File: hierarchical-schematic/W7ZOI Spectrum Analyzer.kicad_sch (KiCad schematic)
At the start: 0 parts

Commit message: improvements to hierarchical schematic
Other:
- note added: ".options gmin=1e-10 .options abstol=1e-10 .tran 10m 500m"
- note added: ".param Rt=10k set=0.9 .param Rt2=10k set2=0.5 .param Rt3=5k set3=0.5 .param Rt4=10k set4=0.9 .param Rt5=5k set5=0.9 .param Rt6=5k set6=0.5"
- note added: "Settings for Pots"
- note added: "Simulation Commands"
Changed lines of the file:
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@@
     (comment 4 "Original Design By:")
   )
-  (image (at 82.55 54.61) (scale 0.801488)
+  (polyline (pts (xy 307.34 156.21) (xy 307.34 167.64))
+    (stroke (width 0) (type default) (color 0 0 0 0))
+  )
+  (polyline (pts (xy 279.4 156.21) (xy 279.4 151.13))
+    (stroke (width 0) (type default) (color 0 0 0 0))
+  )
+  (polyline (pts (xy 336.55 157.48) (xy 336.55 167.64))
+    (stroke (width 0) (type default) (color 0 0 0 0))
+  )
+  (polyline (pts (xy 336.55 167.64) (xy 309.88 167.64))
+    (stroke (width 0) (type default) (color 0 0 0 0))
+  )
+  (polyline (pts (xy 307.34 151.13) (xy 307.34 156.21))
+    (stroke (width 0) (type default) (color 0 0 0 0))
+  )
+  (polyline (pts (xy 309.88 157.48) (xy 336.55 157.48))
+    (stroke (width 0) (type default) (color 0 0 0 0))
+  )
+  (polyline (pts (xy 279.4 151.13) (xy 307.34 151.13))
+    (stroke (width 0) (type default) (color 0 0 0 0))
+  )
+  (polyline (pts (xy 309.88 157.48) (xy 309.88 167.64))
+    (stroke (width 0) (type default) (color 0 0 0 0))
+  )
+  (polyline (pts (xy 279.4 156.21) (xy 279.4 167.64))
+    (stroke (width 0) (type default) (color 0 0 0 0))
+  )
+  (polyline (pts (xy 307.34 167.64) (xy 279.4 167.64))
+    (stroke (width 0) (type default) (color 0 0 0 0))
+  )
+  (image (at 86.36 158.75) (scale 0.801488)
     (data
       iVBORw0KGgoAAAANSUhEUgAAB8AAAASGCAIAAADZyyOxAAAAA3NCSVQICAjb4U/gAAAACXBIWXMA
@@
     )
   )
-  (hierarchical_label "+15" (shape input) (at 237.49 66.04 0)
-    (effects (font (size 1.27 1.27)) (justify left))
+  (text ".options gmin=1e-10\n.options abstol=1e-10\n.tran 10m 500m"
+    (at 312.42 166.37 0)
+    (effects (font (size 1.27 1.27)) (justify left bottom))
   )
-  (hierarchical_label "-15v" (shape input) (at 237.49 91.44 0)
-    (effects (font (size 1.27 1.27)) (justify left))
+  (text ".param Rt=10k set=0.9\n.param Rt2=10k set2=0.5\n.param Rt3=5k set3=0.5\n.param Rt4=10k set4=0.9\n.param Rt5=5k set5=0.9\n.param Rt6=5k set6=0.5\n"
+    (at 280.67 166.37 0)
+    (effects (font (size 1.27 1.27)) (justify left bottom))
   )
-  (sheet (at 166.37 120.65) (size 33.02 39.37) (fields_autoplaced)
+  (text "Simulation Commands" (at 312.42 160.02 0)
+    (effects (font (size 1.27 1.27) (thickness 0.254) bold) (justify left bottom))
+  )
+  (text "Settings for Pots" (at 280.67 153.67 0)
+    (effects (font (size 1.27 1.27) (thickness 0.254) bold) (justify left bottom))
+  )
+  (sheet (at 161.29 22.86) (size 33.02 39.37) (fields_autoplaced)
     (stroke (width 0.254) (type solid) (color 255 0 255 1))
     (fill (color 132 132 0 1.0000))
-    (property "Sheet name" "Resolution Filters" (id 0) (at 166.37 119.9384 0)
+    (property "Sheet name" "Resolution Filters" (id 0) (at 161.29 22.1484 0)
       (effects (font (size 2.54 2.54)) (justify left bottom))
     )
-    (property "Sheet file" "Resolution Filters.kicad_sch" (id 1) (at 166.37 160.6046 0)
+    (property "Sheet file" "Resolution Filters.kicad_sch" (id 1) (at 161.29 62.8146 0)
       (effects (font (size 1.905 1.905)) (justify left top))
     )
   )
-  (sheet (at 234.95 59.69) (size 31.75 40.64) (fields_autoplaced)
+  (sheet (at 19.05 22.86) (size 30.48 39.37) (fields_autoplaced)
     (stroke (width 0.254) (type solid) (color 255 0 255 1))
     (fill (color 194 194 194 1.0000))
-    (property "Sheet name" "15v-power-supply" (id 0) (at 234.95 58.2926 0)
+    (property "Sheet name" "15v-power-supply" (id 0) (at 19.05 21.4626 0)
       (effects (font (size 2.54 2.54)) (justify left bottom))
     )
-    (property "Sheet file" "15v-power-supply.kicad_sch" (id 1) (at 234.95 101.2194 0)
+    (property "Sheet file" "15v-power-supply.kicad_sch" (id 1) (at 19.05 63.1194 0)
       (effects (font (size 1.905 1.905)) (justify left top))
     )
   )
-  (sheet (at 240.03 120.65) (size 33.02 39.37)
+  (sheet (at 223.52 22.86) (size 33.02 39.37)
     (stroke (width 0.254) (type solid) (color 255 0 255 1))
     (fill (color 132 132 0 1.0000))
-    (property "Sheet name" "IF and Log Amplifier" (id 0) (at 237.49 118.11 0)
+    (property "Sheet name" "IF and Log Amplifier" (id 0) (at 220.98 20.32 0)
       (effects (font (size 2.54 2.54)) (justify left bottom))
     )
-    (property "Sheet file" "if_log_amplifier.kicad_sch" (id 1) (at 234.95 162.56 0)
+    (property "Sheet file" "if_log_amplifier.kicad_sch" (id 1) (at 218.44 64.77 0)
       (effects (font (size 1.905 1.905)) (justify left top))
     )
   )
-  (sheet (at 21.59 132.08) (size 33.02 39.37)
+  (sheet (at 91.44 22.86) (size 33.02 39.37)
     (stroke (width 0.254) (type solid) (color 255 0 255 1))
     (fill (color 132 132 0 1.0000))
-    (property "Sheet name" "TimeBase" (id 0) (at 29.21 129.54 0)
+    (property "Sheet name" "TimeBase" (id 0) (at 99.06 20.32 0)
       (effects (font (size 2.54 2.54)) (justify left bottom))
     )
-    (property "Sheet file" "Timebase.kicad_sch" (id 1) (at 21.59 172.0346 0)
+    (property "Sheet file" "Timebase.kicad_sch" (id 1) (at 91.44 62.8146 0)
       (effects (font (size 1.905 1.905)) (justify left top))
     )
@@
       (reference "#PWR015") (unit 1) (value "GND") (footprint "")
     )
-    (path "/e5c5d6b0-703e-4a07-baca-024b54565ece/51c873db-0602-4fbf-b5f8-9bb8f65d1d74"
-      (reference "#PWR016") (unit 1) (value "GND") (footprint "")
-    )
     (path "/e5c5d6b0-703e-4a07-baca-024b54565ece/fe7f195b-9cc7-4d46-8981-0f7c963b0ae9"
       (reference "#PWR017") (unit 1) (value "GND") (footprint "")
@@
       (reference "#PWR018") (unit 1) (value "GND") (footprint "")
     )
-    (path "/e5c5d6b0-703e-4a07-baca-024b54565ece/f54a71f5-08a5-4c9f-abde-53f63c58ed5a"
-      (reference "#PWR019") (unit 1) (value "GND") (footprint "")
-    )
     (path "/e5c5d6b0-703e-4a07-baca-024b54565ece/17e4b05a-5b73-49c6-acba-a1c88a40b2b6"
       (reference "#PWR020") (unit 1) (value "GND") (footprint "")
@@
       (reference "#PWR022") (unit 1) (value "GND") (footprint "")
     )
-    (path "/e5c5d6b0-703e-4a07-baca-024b54565ece/cdaa8220-cb85-4081-8cd8-3498c13d0ae9"
-      (reference "#PWR023") (unit 1) (value "GND") (footprint "")
-    )
-    (path "/e5c5d6b0-703e-4a07-baca-024b54565ece/9a78f27f-8ebb-4899-a8d0-5136e40e60a5"
-      (reference "#PWR0101") (unit 1) (value "GND") (footprint "")
-    )
-    (path "/e5c5d6b0-703e-4a07-baca-024b54565ece/4d49c78c-fd0e-4050-82e0-9a8cb921086d"
-      (reference "#PWR0102") (unit 1) (value "GND") (footprint "")
-    )
     (path "/91afdbb9-c6d6-4a76-a186-be607f7c2a6b/560c3dbb-ab57-471f-8d71-d3e427376a37"
       (reference "#PWR0103") (unit 1) (value "GND") (footprint "")
@@
       (reference "F901") (unit 1) (value "0.5A") (footprint "")
     )
-    (path "/e5c5d6b0-703e-4a07-baca-024b54565ece/a5e98d84-d1a7-44fd-8f2a-8c243a582d46"
-      (reference "H1") (unit 1) (value "MountingHole_Pad") (footprint "MountingHole:MountingHole_2.7mm_M2.5_DIN965_Pad_TopOnly")
-    )
-    (path "/e5c5d6b0-703e-4a07-baca-024b54565ece/b87c65c9-ec3b-45ea-90f3-95476eea7d52"
-      (reference "H2") (unit 1) (value "MountingHole_Pad") (footprint "MountingHole:MountingHole_2.7mm_M2.5_DIN965_Pad_TopOnly")
-    )
-    (path "/e5c5d6b0-703e-4a07-baca-024b54565ece/a3d597da-707e-4562-8cbb-a972a48b51b1"
-      (reference "H3") (unit 1) (value "MountingHole_Pad") (footprint "MountingHole:MountingHole_2.7mm_M2.5_DIN965_Pad_TopOnly")
-    )
-    (path "/e5c5d6b0-703e-4a07-baca-024b54565ece/5b6e3e2e-b7bd-481d-941d-d5bc38f60f37"
-      (reference "H4") (unit 1) (value "MountingHole_Pad") (footprint "MountingHole:MountingHole_2.7mm_M2.5_DIN965_Pad_TopOnly")
-    )
     (path "/633a963b-5ac6-4181-b149-baaec0e755c1/aaab055d-e2c8-47ec-bf52-ba6cbf89c068"
       (reference "H901") (unit 1) (value "MountingHole") (footprint "MountingHole:MountingHole_3.2mm_M3")
@@
       (reference "J9") (unit 1) (value "Conn_Coaxial") (footprint "SnapEDA Library:TE_5-1634503-1")
     )
-    (path "/e5c5d6b0-703e-4a07-baca-024b54565ece/eeba3f92-201a-4f56-afb1-a990ad9a518a"
-      (reference "J402") (unit 1) (value "Jack-DC") (footprint "SnapEDA Library:CUI_PJ-007")
-    )
-    (path "/e5c5d6b0-703e-4a07-baca-024b54565ece/828929ad-f86d-4271-8167-d5d47d1d234b"
-      (reference "J404") (unit 1) (value "Jack-DC") (footprint "SnapEDA Library:CUI_PJ-007")
-    )
     (path "/1213119d-b3ea-47c8-aaf6-ecc398bfbb00/5c2fd91a-2547-4d62-bb9f-a69cddcb397b"
       (reference "J501") (unit 1) (value "Conn_Coaxial") (footprint "")
@@
       (reference "U902") (unit 1) (value "LM7915") (footprint "Package_TO_SOT_THT:TO-220-3_Horizontal_TabUp")
     )
-    (path "/e5c5d6b0-703e-4a07-baca-024b54565ece/663fb189-de49-422b-ad38-7d7dade67ea7"
-      (reference "V401") (unit 1) (value "DC 15") (footprint "SnapEDA Library:CUI_PJ-009A")
-    )
-    (path "/e5c5d6b0-703e-4a07-baca-024b54565ece/1cda291b-3970-4d26-9e57-945fdd846461"
-      (reference "V402") (unit 1) (value "DC -15") (footprint "SnapEDA Library:CUI_PJ-009A")
-    )
     (path "/1213119d-b3ea-47c8-aaf6-ecc398bfbb00/1a05bef1-a2a6-4cee-a2ef-ce4abb0dcdfa"

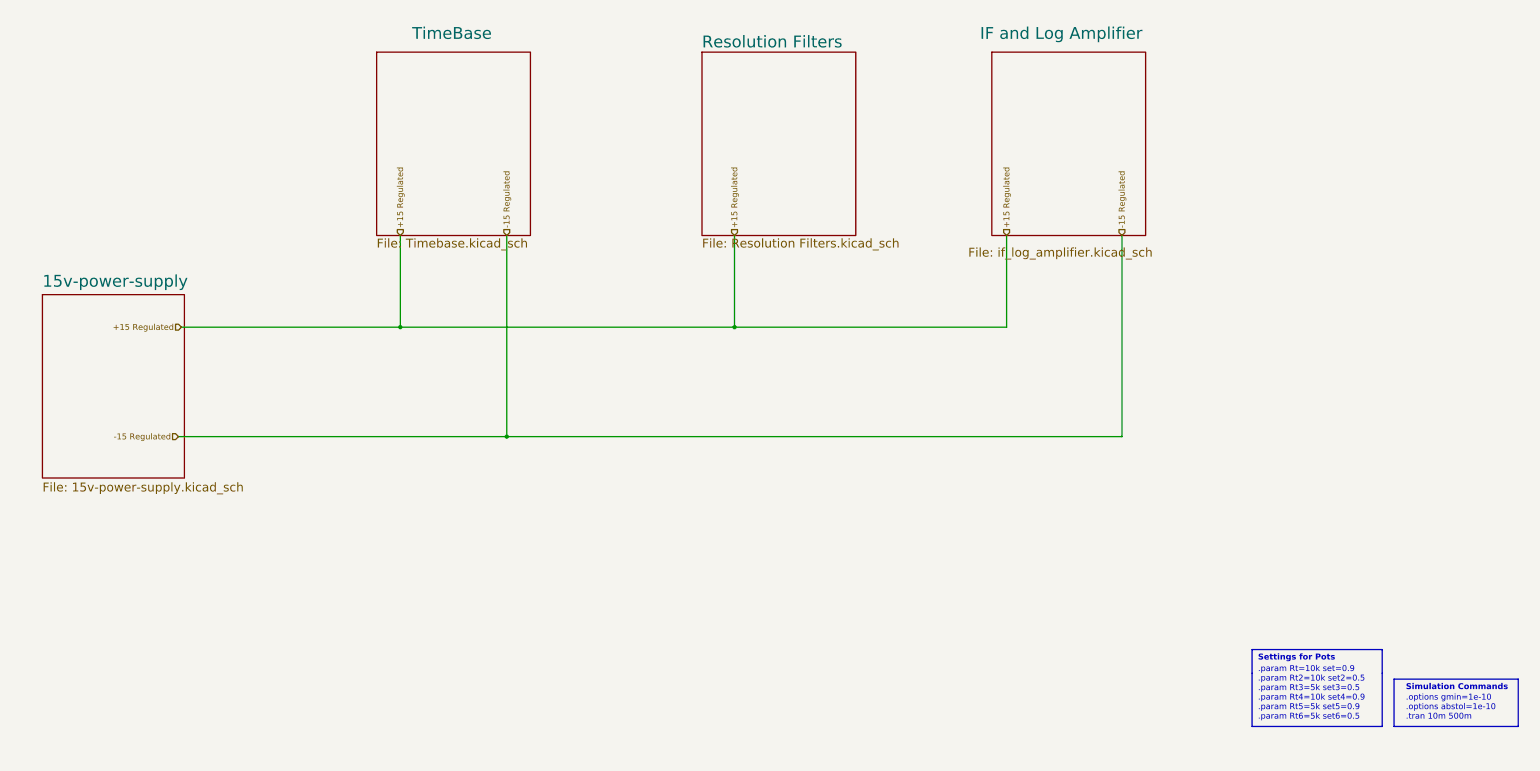
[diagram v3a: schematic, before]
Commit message: improved if and log amp and second lo/mixer
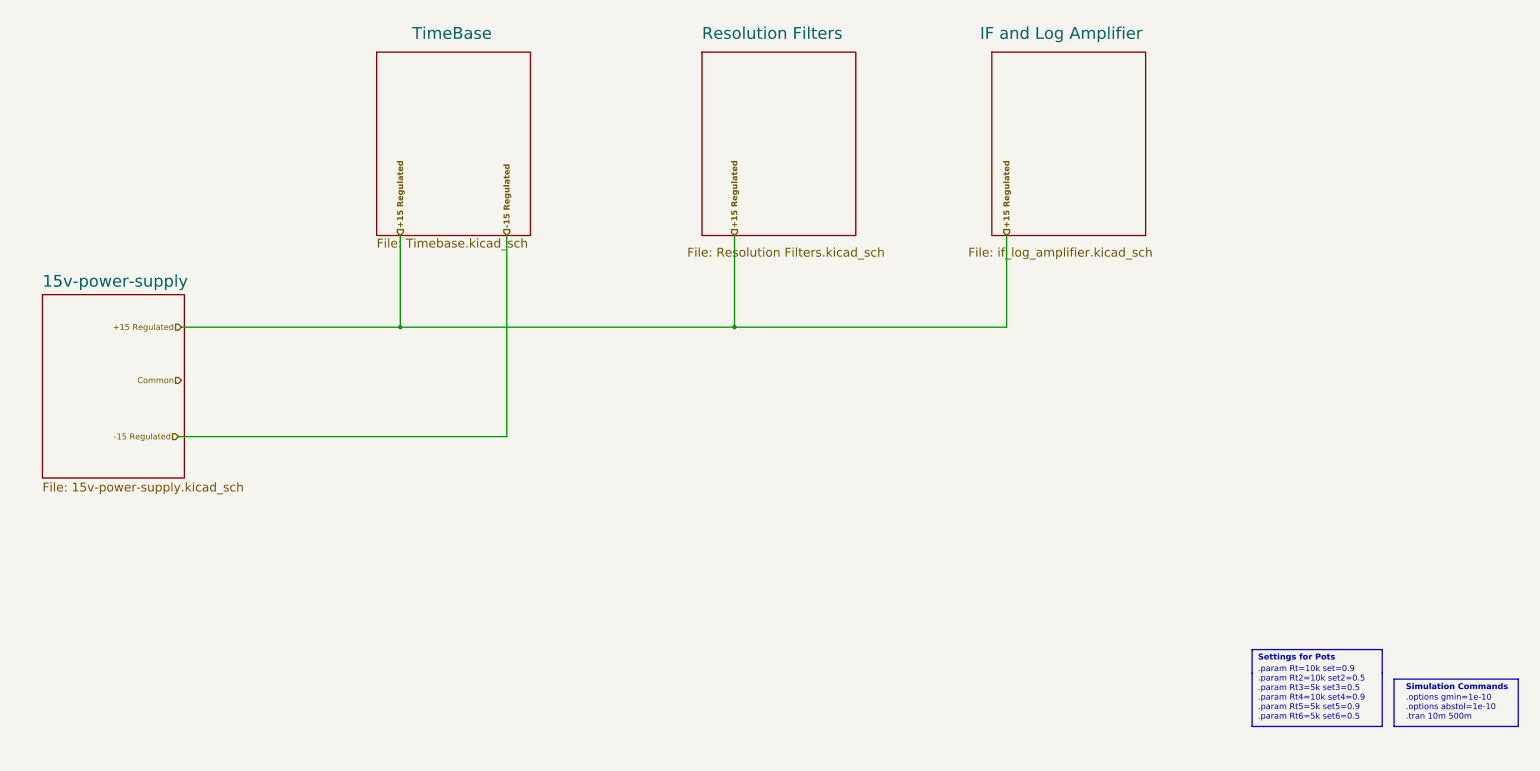
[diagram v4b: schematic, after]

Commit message: minor fix to 2ndmixer-2ndlo
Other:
- added sheet 2nd Mixer 2nd LO (2ndmixer-2ndlo.kicad_sch)

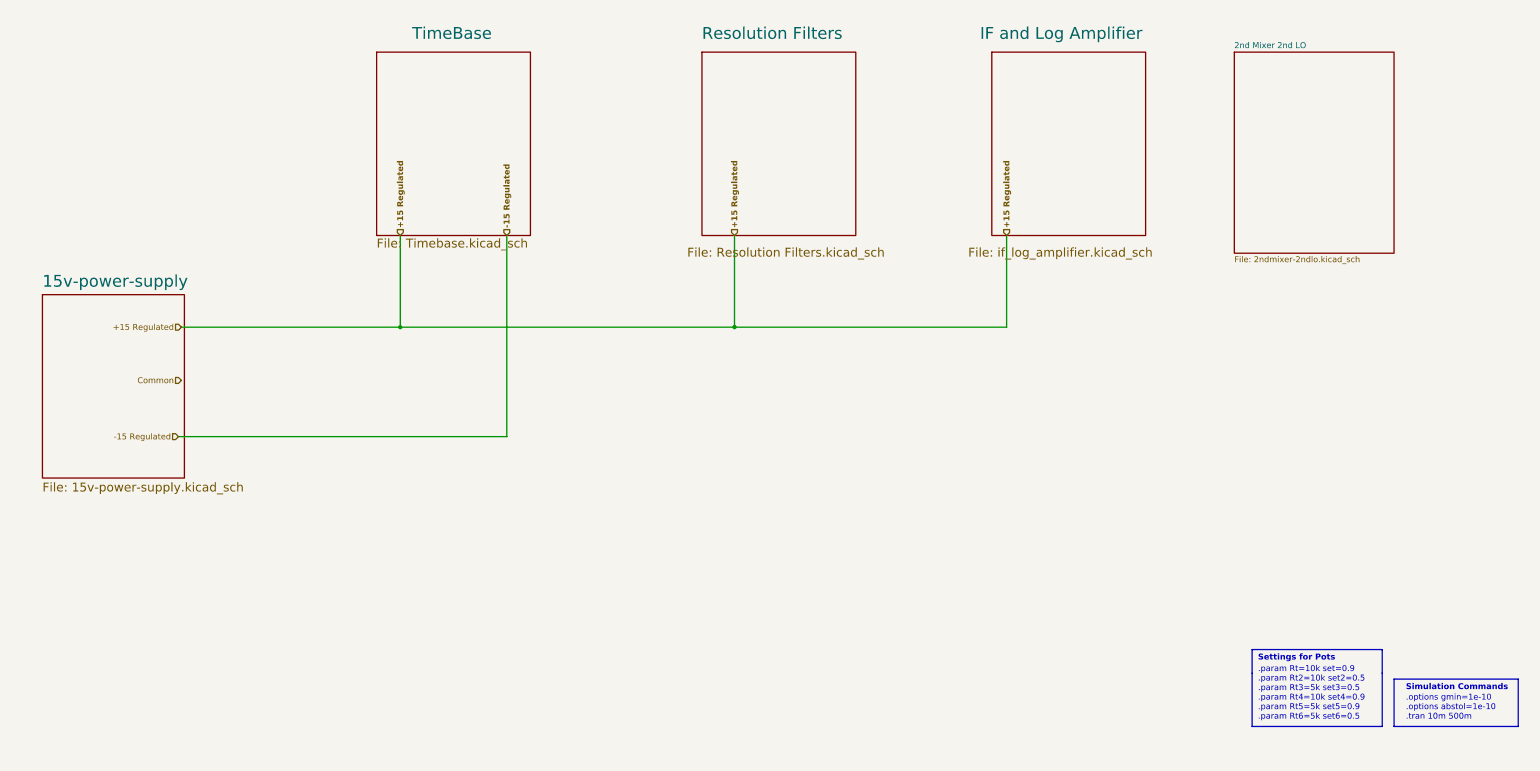
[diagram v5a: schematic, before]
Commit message: Hierarchical schematic updates
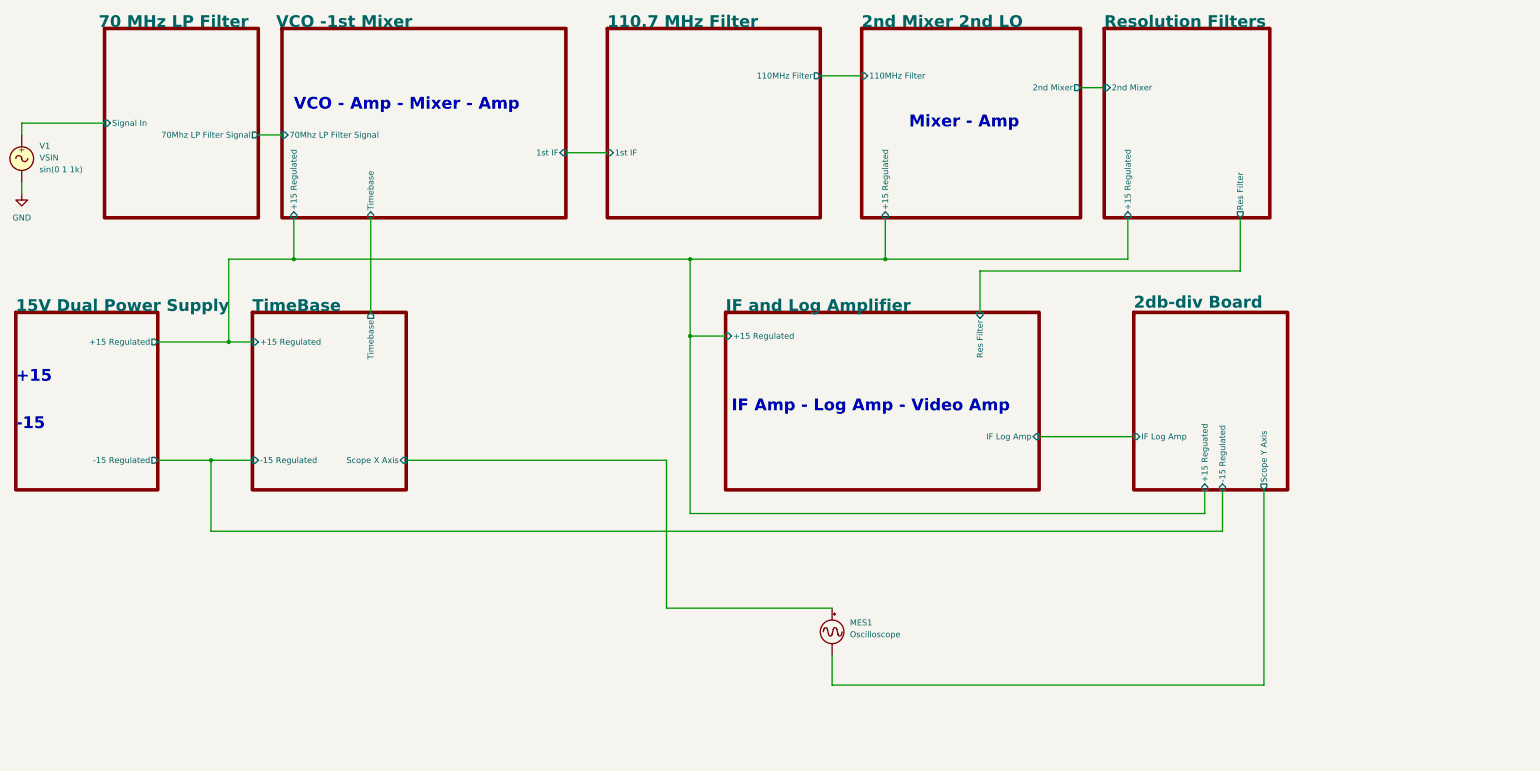
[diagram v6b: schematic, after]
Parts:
- added MES1: Oscilloscope, symbol Device:Oscilloscope
- added V1: VSIN, symbol Simulation_SPICE:VSIN
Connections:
- new net 2db-div Board/Scope Y Axis: MES1.1 (-)
- new net 70 MHz LP Filter/Signal In: V1.1
- new net GND: V1.2
- new net TimeBase/Scope X Axis: MES1.2 (+)
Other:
- sheet 15v-power-supply renamed 15V Dual Power Supply
- added sheet 110.7 MHz Filter (110_7mhz-filter.kicad_sch)
- added sheet 2db-div Board (2db-div.kicad_sch)
- added sheet 70 MHz LP Filter (70mhz-lpfilter.kicad_sch)
- added sheet VCO -1st Mixer (vco-1stmixer.kicad_sch)
- sheet 15V Dual Power Supply ports: added +15 Regulated, -15 Regulated; removed none
- sheet 2nd Mixer 2nd LO ports: added +15 Regulated, 110MHz Filter, 2nd Mixer; removed none
- sheet IF and Log Amplifier ports: added +15 Regulated, IF Log Amp, Res Filter; removed none
- sheet Resolution Filters ports: added +15 Regulated, 2nd Mixer, Res Filter; removed none
- sheet TimeBase ports: added +15 Regulated, -15 Regulated, Scope X Axis, Timebase; removed none
- note added: "+15"
- note added: "-15"
- note added: "IF Amp - Log Amp - Video Amp"
- note added: "Mixer - Amp"
- note added: "VCO - Amp - Mixer - Amp"
- note removed: ".options gmin=1e-10 .options abstol=1e-10 .tran 10m 500m"
- note removed: ".param Rt=10k set=0.9 .param Rt2=10k set2=0.5 .param Rt3=5k set3=0.5 .param Rt4=10k set4=0.9 .param Rt5=5k set5=0.9 .param Rt6=5k set6=0.5"
- note removed: "Settings for Pots"
- note removed: "Simulation Commands"
